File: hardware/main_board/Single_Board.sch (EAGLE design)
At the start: 47 parts, among them J1 5520425-3, J2 U.FL, J3 AVR_SPI_PROG_3X2NS, Q1 220mA/50V/3.5Ω, Q2 220mA/50V/3.5Ω, U1 INA199A3DCKR, U2 MCP1703T-3302E/CB, U3 W25X40CLSNIG, U5 ATMEGA328PB-AU, X1 32.768KHZ-FC-135, X2 B2B-PH-K-S, X3 B2B-XH-2

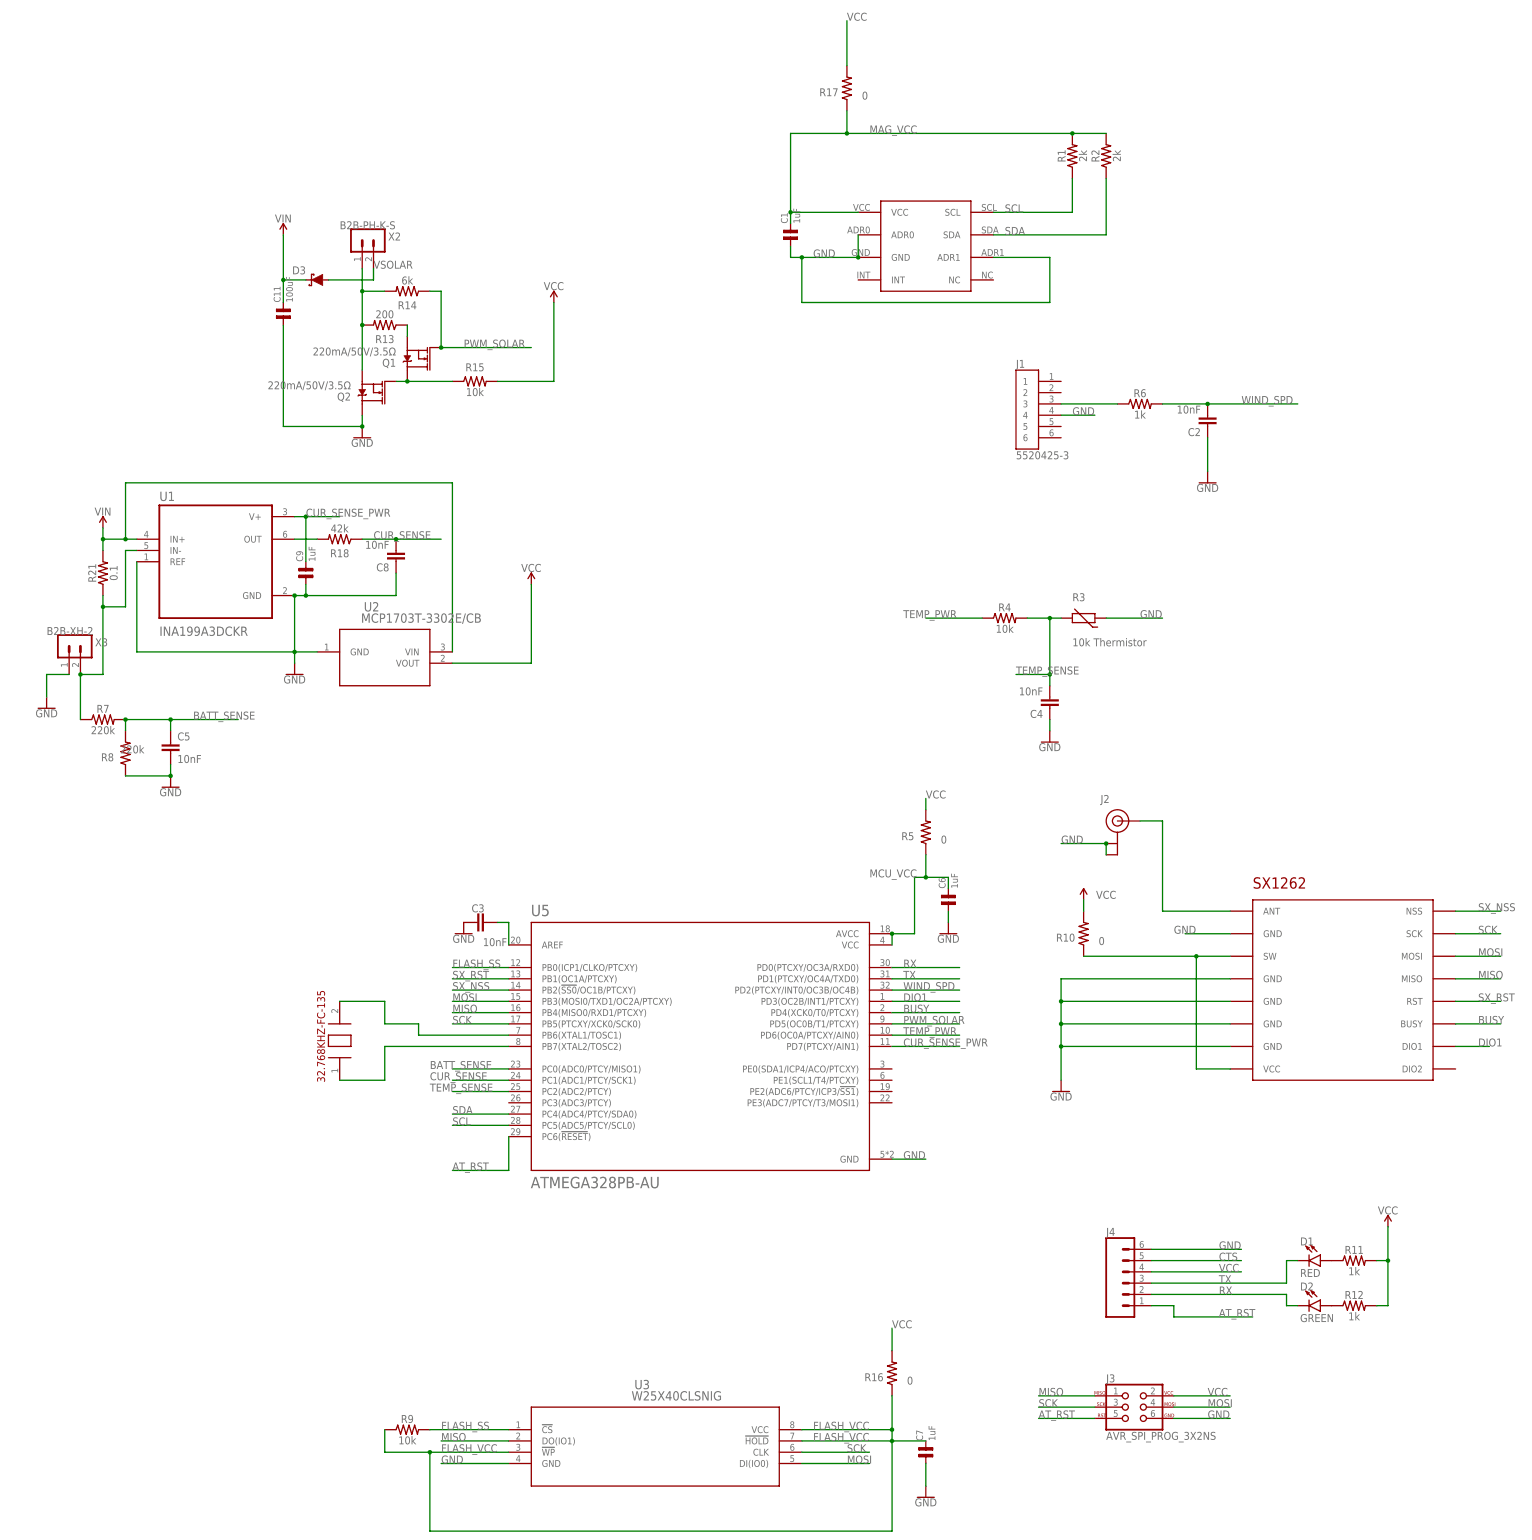
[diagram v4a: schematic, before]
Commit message: Added config for new board Updated Solar PWM for current sensor and impedance switching Fixed a bug with internal termperature sense Added more charge info to detailed weather messages Added support for AVRISP programmer Finalized new board
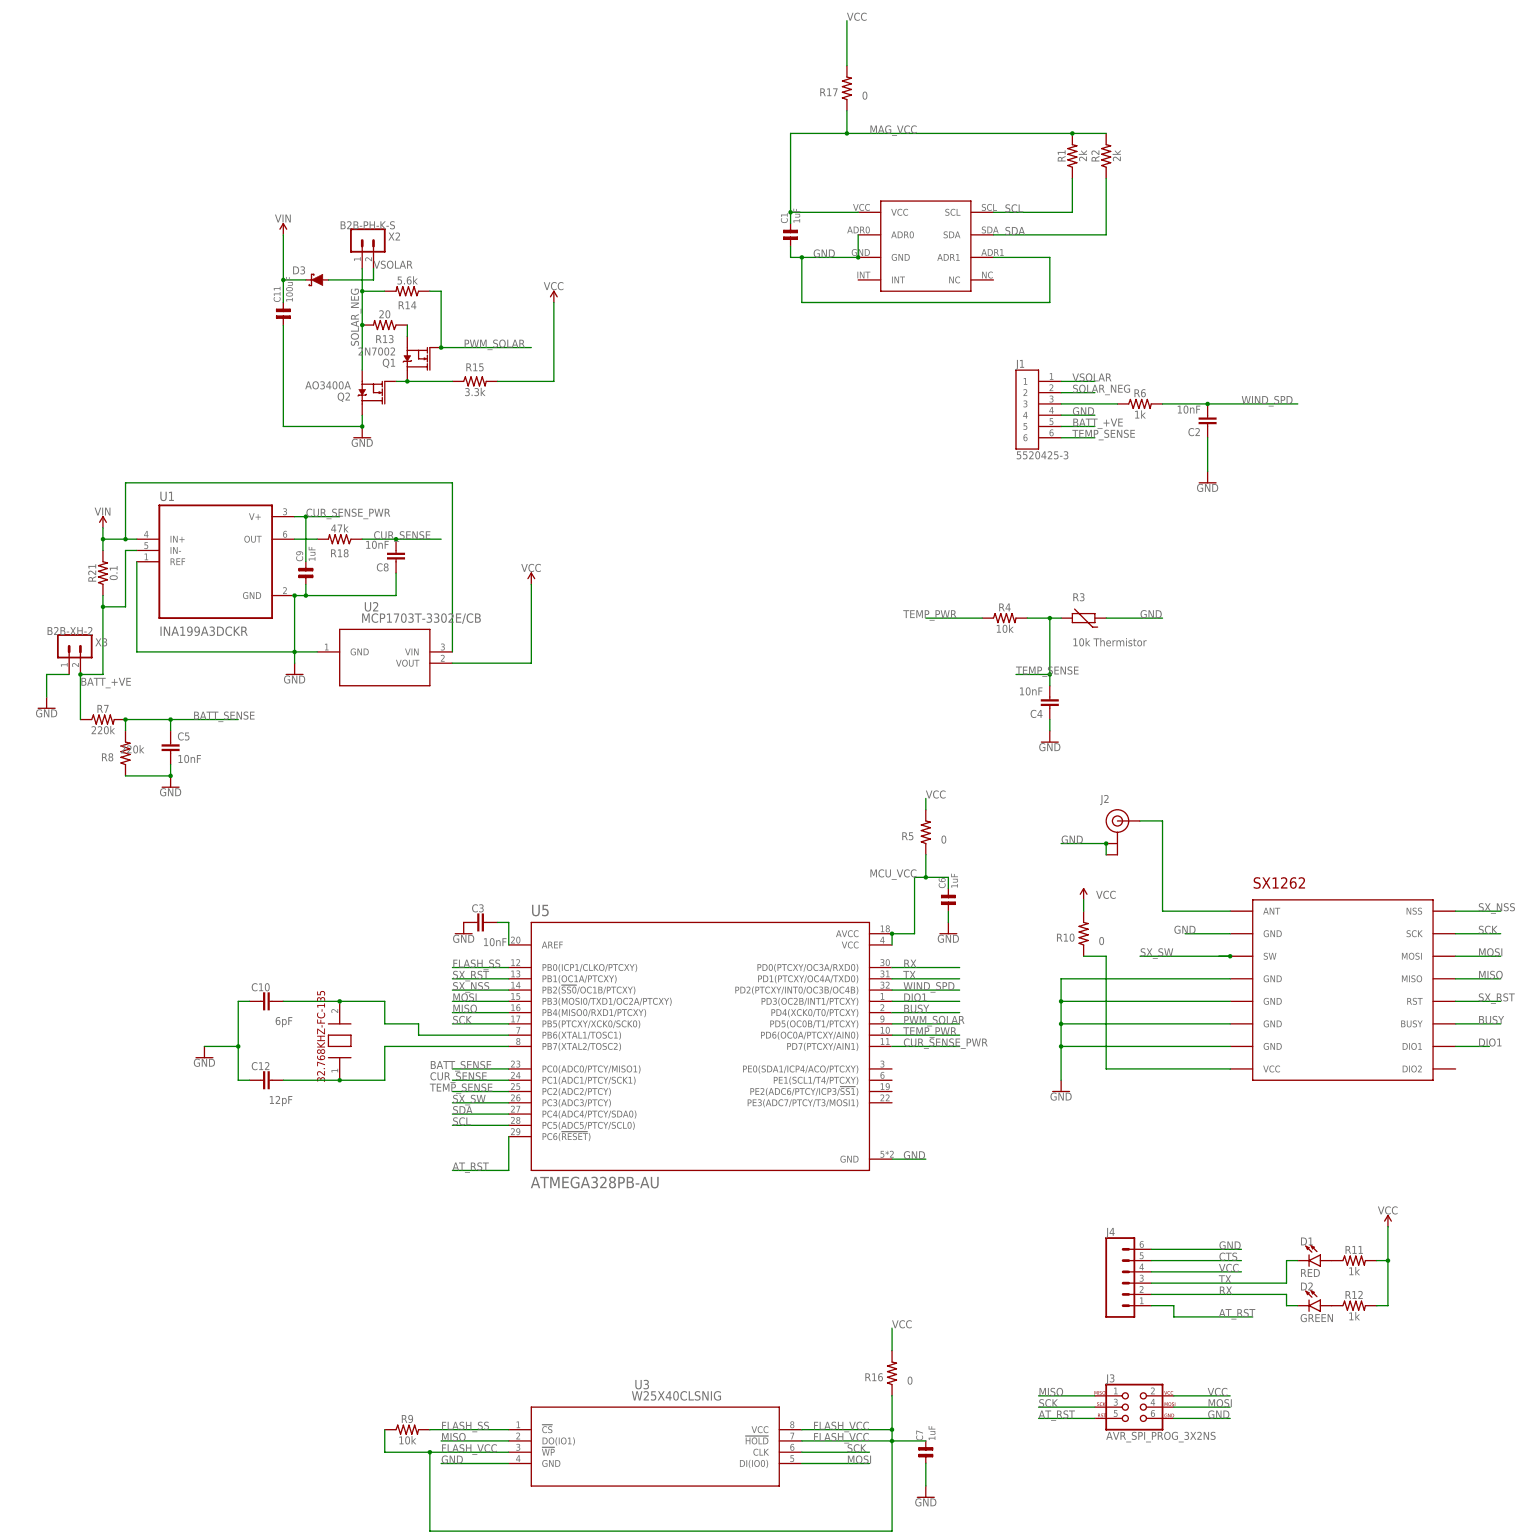
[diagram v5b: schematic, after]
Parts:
- added C10: 6pF, SparkFun-Capacitors:10NF-0603-50V-10%
- added C12: 12pF, SparkFun-Capacitors:10NF-0603-50V-10%
- D3: value 0.5A/40V/420mV -> NSR0240HT1G
- Q1: value 220mA/50V/3.5Ω -> 2N7002
- Q2: value 220mA/50V/3.5Ω -> AO3400A
- R13: value 200 -> 20
- R14: value 6k -> 5.6k
- R15: value 10k -> 3.3k
- R18: value 42k -> 47k
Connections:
- removed net N$11: R21.1, R7.1, U1.IN-, X3.2
- removed net N$9: Q2.S, R13.2, R14.2, X2.1
- new net BATT_+VE: J1.5, R21.1, R7.1, U1.IN-, X3.2
- new net SOLAR_NEG: J1.2, Q2.S, R13.2, R14.2, X2.1
- new net SX_SW: U$2.SW, U5.PC3(ADC3/PTCY)
- net GND: now also C10.1, C12.1
- net N$1: no longer U$2.SW
- net N$7: now also C10.2
- net N$8: now also C12.2
- net TEMP_SENSE: now also J1.6
- net VSOLAR: now also J1.1

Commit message: Board improvements: Current sensor less prone to latchup Reset pull up resistor JST SH battery connector 8p8c connector to remove shared grounds NPN transistor so we don't operate the mcu outside of spec
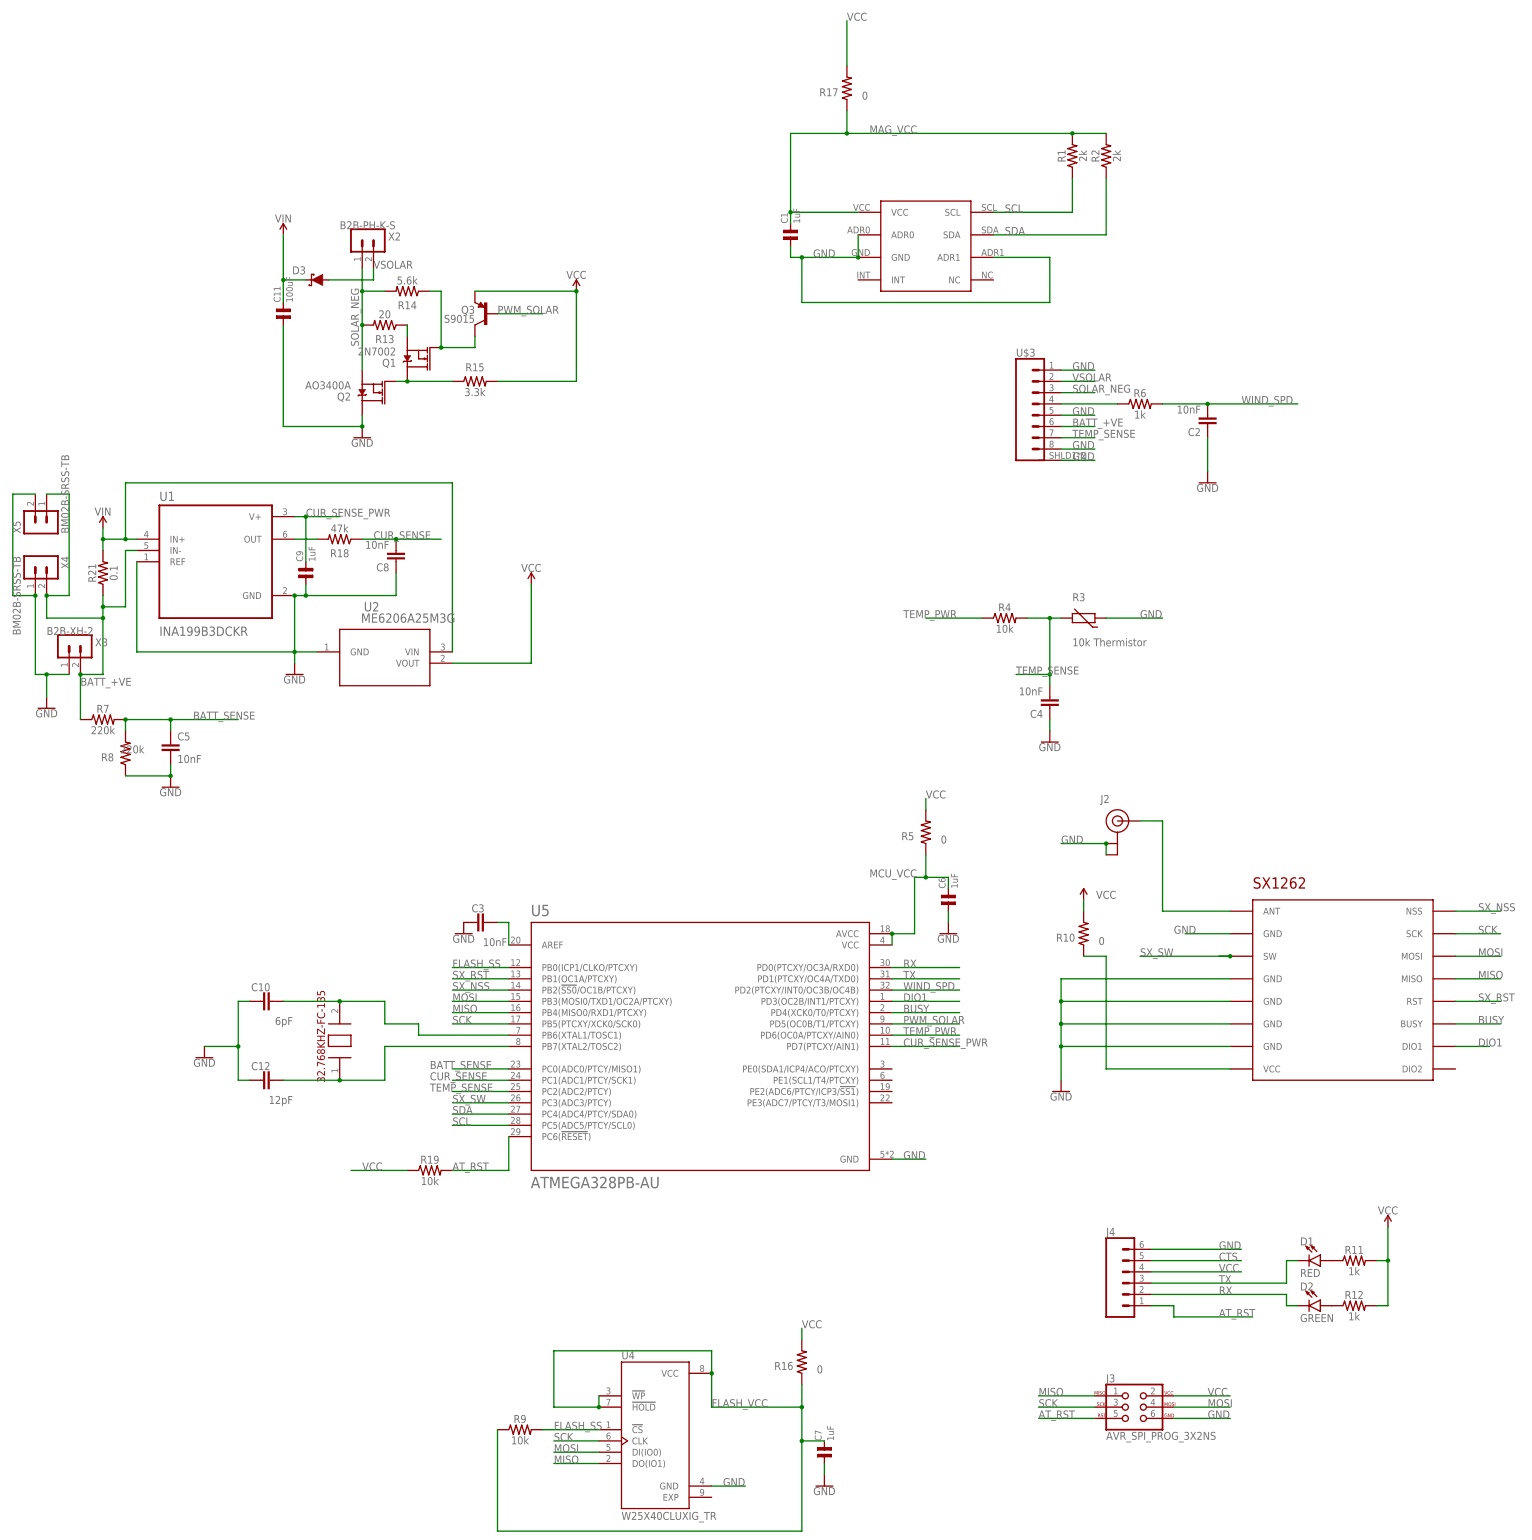
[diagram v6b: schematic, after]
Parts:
- removed J1: 5520425-3, main_board:5520425-3
- removed U3: W25X40CLSNIG, my-components:W25X40CLSNIG
- added Q3: S9015, SparkFun-DiscreteSemi:TRANS_PNP-MMBT4403
- added R19: 10k, SparkFun-Resistors:RESISTOR0805
- added U$3: (no value), main_board:RJSHE3380
- added U4: W25X40CLUXIG_TR, main_board:W25X40CLUXIG_TR
- added X4, X5: BM02B-SRSS-TB, main_board:BM02B-SRSS-TB
- U1: value INA199A3DCKR -> INA199B3DCKR
- U2: value MCP1703T-3302E/CB -> ME6206A25M3G
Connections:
- new net N$11: Q1.G, Q3.C, R14.1
- net AT_RST: now also R19.2
- net BATT_+VE: now also U$3.6, X4.2, X5.1; no longer J1.5
- net FLASH_SS: now also U4.!CS; no longer U3.!CS
- net FLASH_VCC: now also U4.!HOLD, U4.!WP, U4.VCC; no longer U3.!HOLD, U3.!WP, U3.VCC
- net GND: now also U$3.1, U$3.5, U$3.8, U$3.SHLD, U4.GND, X4.1, X5.2; no longer J1.4, U3.GND
- net MISO: now also U4.DO(IO1); no longer U3.DO(IO1)
- net MOSI: now also U4.DI(IO0); no longer U3.DI(IO0)
- net N$16: now also U$3.4; no longer J1.3
- net PWM_SOLAR: now also Q3.B; no longer Q1.G, R14.1
- net SCK: now also U4.CLK; no longer U3.CLK
- net SOLAR_NEG: now also U$3.3; no longer J1.2
- net TEMP_SENSE: now also U$3.7; no longer J1.6
- net VCC: now also Q3.E, R19.1
- net VSOLAR: now also U$3.2; no longer J1.1
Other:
- moved on the sheet: C7, R16, R9
